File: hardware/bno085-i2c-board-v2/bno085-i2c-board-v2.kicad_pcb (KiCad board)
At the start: 2 copper layers, 13 parts, among them J1 Conn_01x01_Pin, J2 Conn_01x01_Pin, J3 Conn_01x01_Pin, J4 Conn_01x01_Pin, J5 Conn_01x01_Pin, J6 Conn_01x01_Pin

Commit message: pcb
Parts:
- moved C1 27.2 mm to (188.8, 103.8)
- moved R1 20.3 mm to (178.9, 94.5), turned to 0 degrees
- moved R2 16.2 mm to (178.9, 96.5)
- moved J1 15.3 mm to (174.0, 97.0)
- moved J2 13.5 mm to (174.0, 103.0)
- moved R3 13.1 mm to (178.9, 98.5)
- moved J5 11.9 mm to (170.0, 105.5)
- moved J4 11.5 mm to (170.0, 94.5)
- moved R4 10.1 mm to (178.9, 100.5)
- moved R5 9.93 mm to (178.9, 102.5), turned to 0 degrees
- moved J3 7.38 mm to (165.5, 97.0)
- moved U1 6.97 mm to (169.8, 100.0), turned to 90 degrees
- moved J6 4.30 mm to (165.5, 103.0)
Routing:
- net +3.3V: track 11.8 -> 0.00 mm
- net Net-(J3-Pin_1): track 5.97 -> 0.00 mm
- net Net-(U1-BOOTN): track 1.18 -> 0.00 mm
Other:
- board outline added: 15 x 15 mm

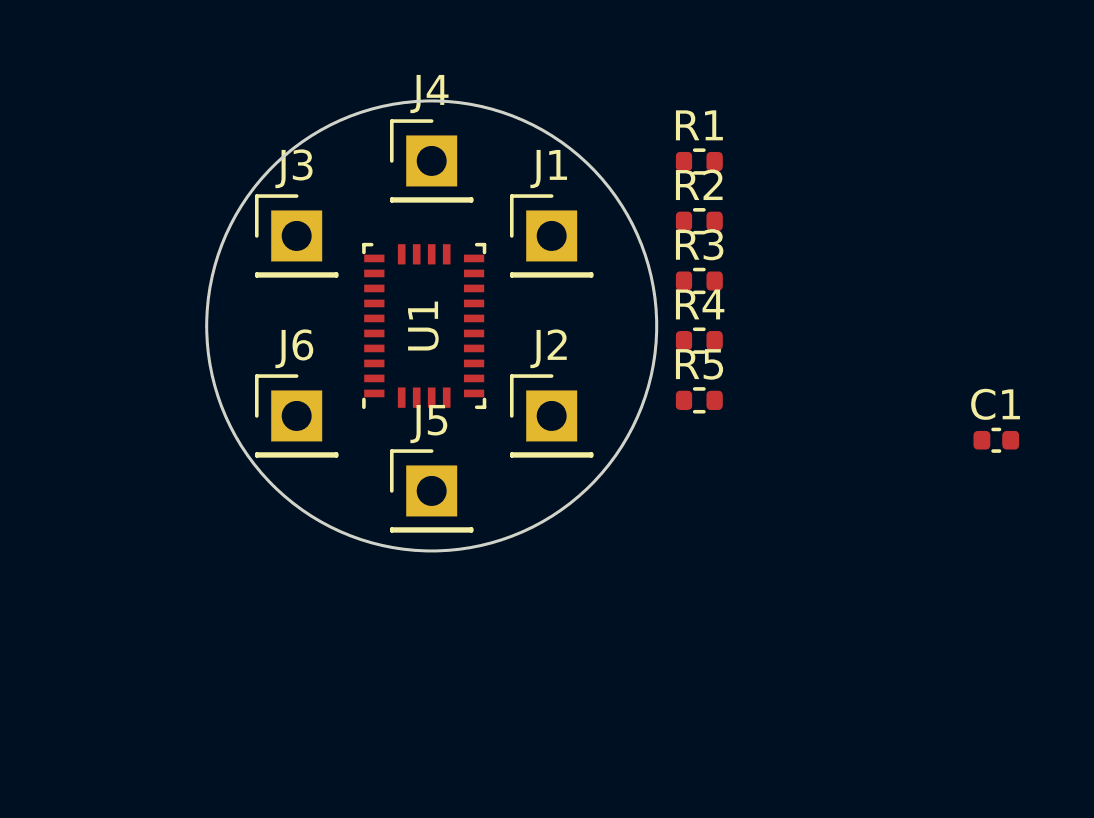
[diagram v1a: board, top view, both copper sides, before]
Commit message: round board
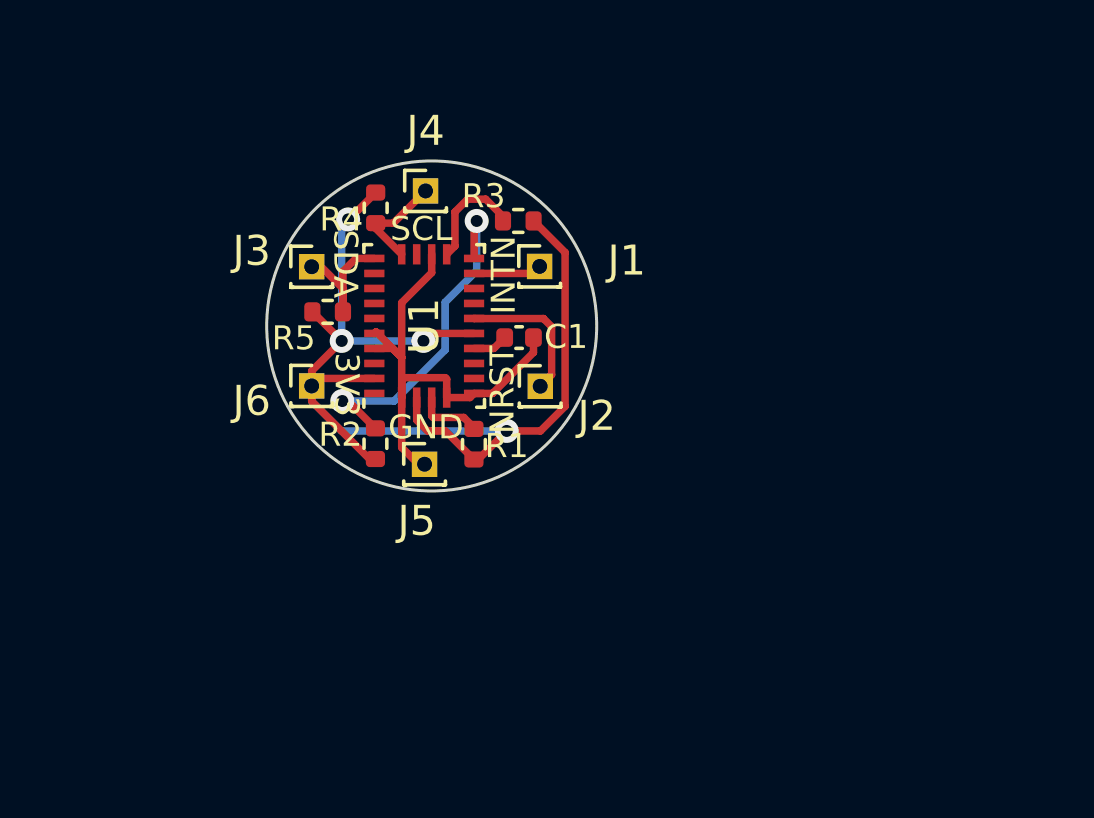
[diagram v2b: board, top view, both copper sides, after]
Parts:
- J1, J2, J3, J4, J5, J6: footprint Connector_PinHeader_2.54mm:PinHeader_1x01_P2.54mm_Vertical -> Connector_PinHeader_1.00mm:PinHeader_1x01_P1.00mm_Vertical
- moved C1 16.3 mm to (172.9, 100.4)
- moved R2 13.1 mm to (168.1, 103.9), turned to 90 degrees
- moved R5 12.7 mm to (166.5, 99.5), turned to 180 degrees
- moved R1 12.0 mm to (171.4, 103.9), turned to -90 degrees
- moved R4 11.7 mm to (168.1, 96.1), turned to -90 degrees
- moved R3 6.36 mm to (172.9, 96.5)
- moved J3 1.14 mm to (166.0, 98.0)
- moved J6 1.12 mm to (166.0, 102.0)
- moved J1 1.09 mm to (173.6, 98.0)
- moved J2 1.06 mm to (173.6, 102.0)
- moved J4 1.02 mm to (169.8, 95.5)
- moved J5 0.92 mm to (169.8, 104.6)
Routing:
- net +3.3V: track 0.00 -> 39.9 mm, vias 0 -> 4
- net GND: track 0.00 -> 17.0 mm
- net Net-(U1-ENV_SCL): track 0.00 -> 11.6 mm, vias 0 -> 2
- net Net-(J2-Pin_1): track 0.00 -> 4.84 mm
- net Net-(J3-Pin_1): track 0.00 -> 4.38 mm
- net Net-(U1-ENV_SDA): track 0.00 -> 3.69 mm
- net Net-(J4-Pin_1): track 0.00 -> 3.51 mm
- net Net-(J1-Pin_1): track 0.00 -> 2.61 mm
- net Net-(U1-BOOTN): track 0.00 -> 2.23 mm
- net Net-(U1-CAP): track 0.00 -> 1.17 mm
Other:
- board size 15 x 15 mm -> 11 x 11 mm
- board text added: "3V3"
- board text added: "GND"
- board text added: "INTN"
- board text added: "NRST"
- board text added: "SCL"
- board text added: "SDA"
